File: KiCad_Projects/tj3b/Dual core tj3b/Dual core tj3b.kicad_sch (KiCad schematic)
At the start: 75 parts

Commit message: 基板データの更新
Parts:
- removed J? (x3): Conn_01x04_Female, Connector_JST:JST_XH_B4B-XH-A_1x04_P2.50mm_Vertical, symbol Connector:Conn_01x04_Female
- removed R? (x4): 10k, Resistor_THT:R_Axial_DIN0204_L3.6mm_D1.6mm_P5.08mm_Horizontal, symbol Device:R
- added J?: Conn_01x06_Female, symbol Connector:Conn_01x06_Female
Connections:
- net AD1: no longer J?.1 (Pin_1), R?.2, U?.2 (RA0/AN0)
- net AD10: no longer J?.1 (Pin_1), R?.2, U?.21 (AN12/INT0/RB0)
- net AD2: no longer J?.1 (Pin_1), R?.2, U?.3 (RA1/AN1)
- net AD3: no longer J?.1 (Pin_1), R?.2, U?.4 (RA2/Vref-AN2)
- net AD4: no longer J?.1 (Pin_1), R?.2, U?.5 (RA3/Vref+AN3)
- net AD5: no longer J?.1 (Pin_1), R?.2, U?.7 (RA5/AN4)
- net AD6: no longer J?.1 (Pin_1), R?.2, U?.23 (AN8/INT2/RB2)
- net AD7: no longer J?.1 (Pin_1), R?.2, U?.24 (AN9/RB3)
- net AD8: no longer J?.1 (Pin_1), R?.2, U?.22 (AN10/INT1/RB1)
- net AD9: no longer J?.1 (Pin_1), R?.2, U?.25 (AN11/RB4)
- net MCLR: no longer U?.1 (~{MCLR}/RE3)
- net MON LED: no longer U?.10 (RA6/OSC2/CLKOUT)
- net PWR LED: no longer U?.9 (RA7/OSC1/CLKIN)
- net RA4: no longer U?.6 (RA4)
- net RX: now also J?.5 (Pin_5); no longer U?.18 (RX/RC7)
- net TX: now also J?.4 (Pin_4); no longer U?.17 (TX/RC6)
- new net AD11: J?.1 (Pin_1), R?.2, U?.2 (RA0/AN0)
- new net AD12: J?.1 (Pin_1), R?.2, U?.3 (RA1/AN1)
- new net AD13: J?.1 (Pin_1), R?.2, U?.4 (RA2/Vref-AN2)
- new net AD14: J?.1 (Pin_1), R?.2, U?.5 (RA3/Vref+AN3)
- new net AD15: J?.1 (Pin_1), R?.2, U?.7 (RA5/AN4)
- new net AD16: J?.1 (Pin_1), R?.2, U?.23 (AN8/INT2/RB2)
- new net AD17: J?.1 (Pin_1), R?.2, U?.24 (AN9/RB3)
- new net AD18: J?.1 (Pin_1), R?.2, U?.22 (AN10/INT1/RB1)
- new net AD19: J?.1 (Pin_1), R?.2, U?.25 (AN11/RB4)
- new net AD20: J?.1 (Pin_1), R?.2, U?.21 (AN12/INT0/RB0)
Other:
- note added: "Main TJ3B"
- note added: "Sirial connector"
- note added: "Slave TJ3B"
- note added: "Type-C to Sirial"
- moved on the sheet: C?, D?, J?, R?, RS?, SS?, U?

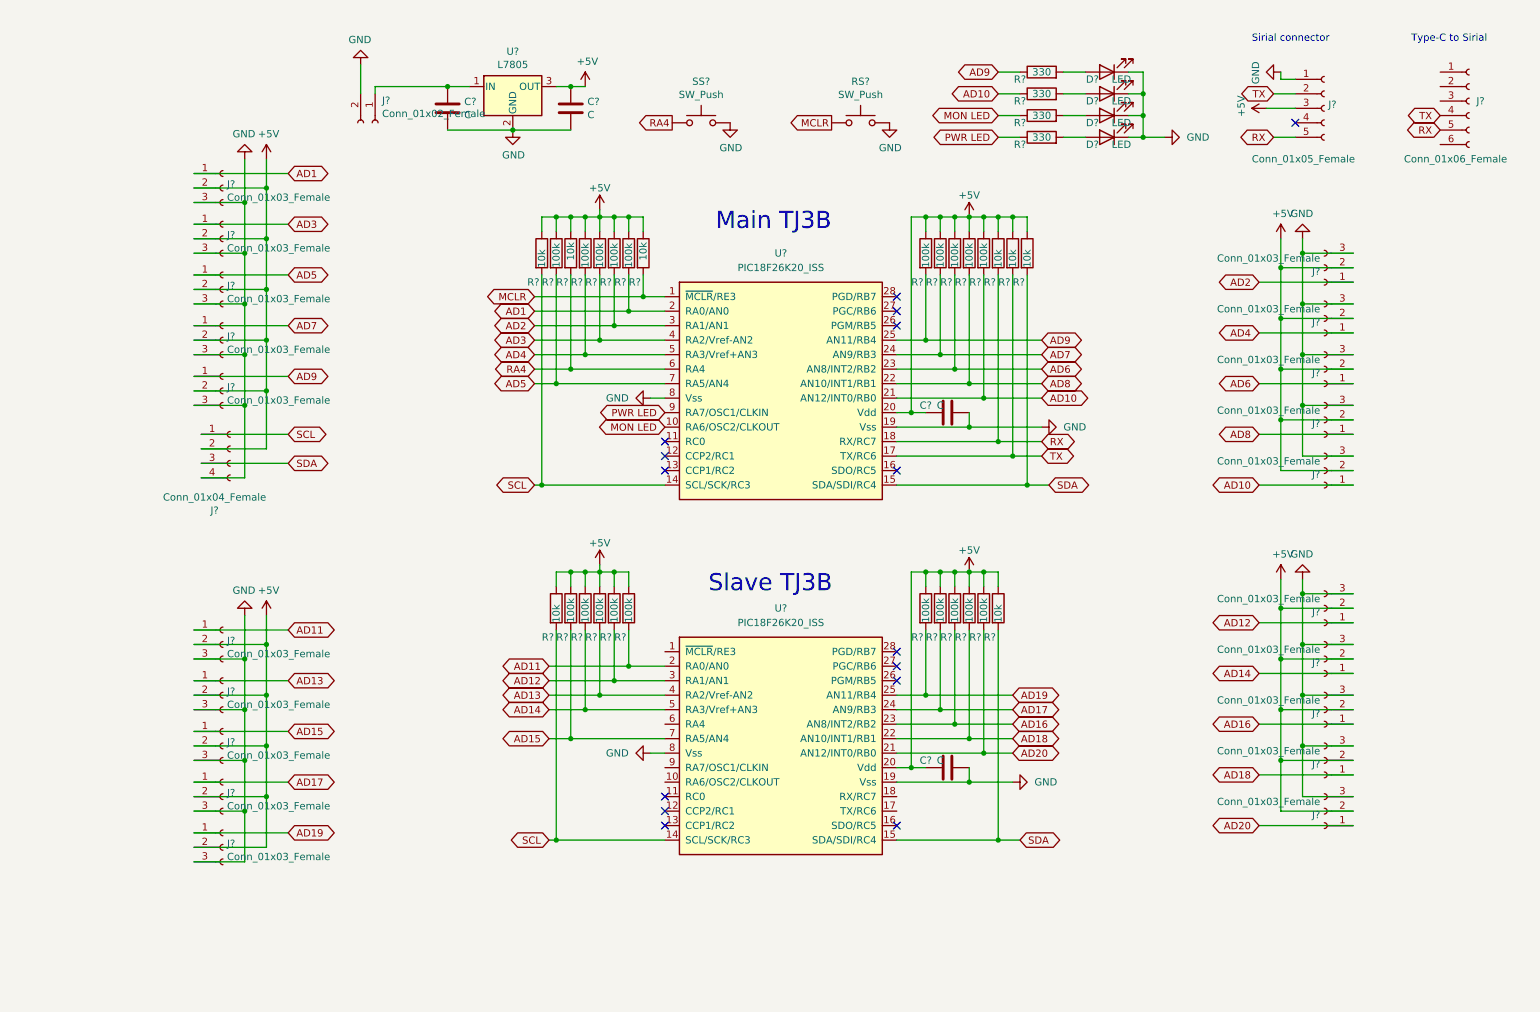
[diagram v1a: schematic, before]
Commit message: ハードのデータ更新
いろいろたまって申し訳ない
ハード全般のデータ更新です。
ついでに、2023シーズン用のプレゼンシートも上げときます。（未完成）
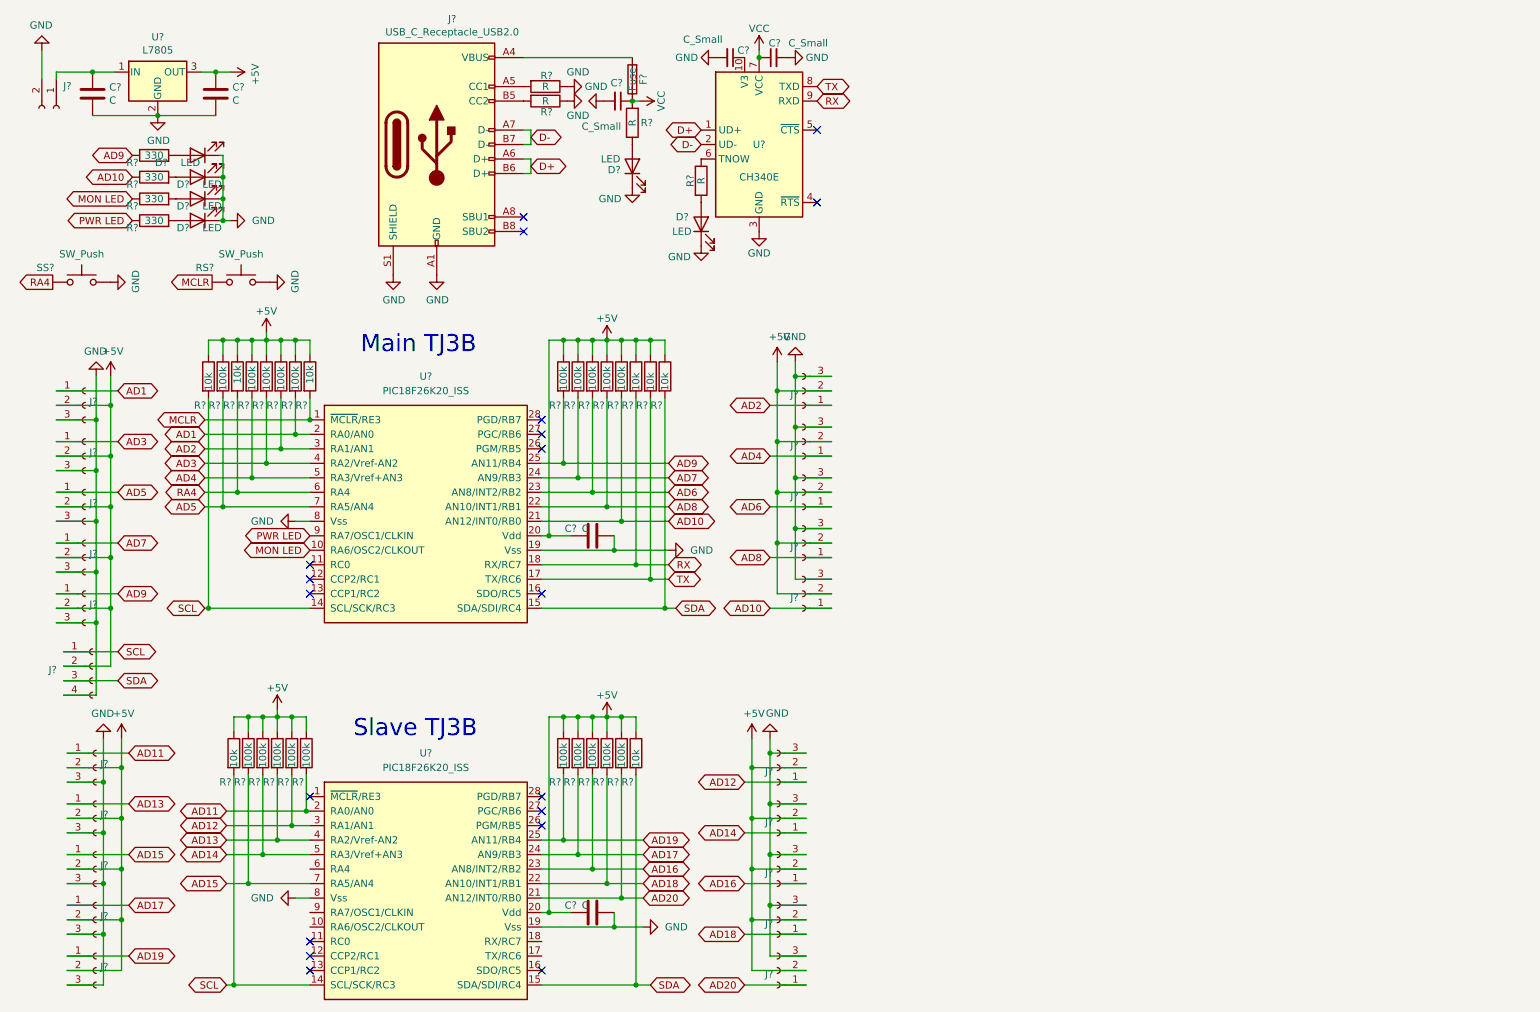
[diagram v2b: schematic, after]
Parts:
- removed J?: Conn_01x05_Female, Connector_JST:JST_XH_B5B-XH-A_1x05_P2.50mm_Vertical, symbol Connector:Conn_01x05_Female
- removed J?: Conn_01x06_Female, symbol Connector:Conn_01x06_Female
- added C? (x3): C_Small, Capacitor_SMD:C_01005_0402Metric, symbol Device:C_Small
- added D? (x2): LED, LED_SMD:LED_0402_1005Metric, symbol Device:LED
- added F?: Fuse, Fuse:Fuse_0603_1608Metric, symbol Device:Fuse
- added J?: USB_C_Receptacle_USB2.0, Connector_USB:USB_C_Receptacle_XKB_U262-16XN-4BVC11, symbol Connector:USB_C_Receptacle_USB2.0
- added R? (x3): R, Resistor_SMD:R_0402_1005Metric, symbol Device:R
- added R?: R, Resistor_SMD:R_0603_1608Metric, symbol Device:R
- added U?: CH340E, Package_SO:MSOP-10_3x3mm_P0.5mm, symbol Interface_USB:CH340E
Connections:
- net GND: now also C?.2, C?.2, C?.2, D?.1 (K), D?.1 (K), J?.A1 (GND), J?.A12 (GND), J?.B1 (GND), J?.B12 (GND), J?.S1 (SHIELD), R?.1, R?.1, U?.3 (GND)
- net RX: now also U?.9 (RXD)
- net TX: now also U?.8 (TXD)
- new net: D?.2 (A), R?.1
- new net: C?.1, U?.10 (V3)
- new net: R?.1, U?.6 (TNOW)
- new net: D?.2 (A), R?.2
- new net: F?.2, J?.A4 (VBUS), J?.A9 (VBUS), J?.B4 (VBUS), J?.B9 (VBUS)
- new net: J?.A5 (CC1), R?.2
- new net: J?.B5 (CC2), R?.2
- new net D+: J?.A6 (D+), J?.B6 (D+), U?.1 (UD+)
- new net D-: J?.A7 (D-), J?.B7 (D-), U?.2 (UD-)
- new net VCC: C?.1, C?.1, F?.1, R?.2, U?.7 (VCC)
- no-connect marks 15 -> 19
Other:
- note removed: "Sirial connector"
- note removed: "Type-C to Sirial"
- moved on the sheet: C?, D?, J?, R?, RS?, SS?, U?
